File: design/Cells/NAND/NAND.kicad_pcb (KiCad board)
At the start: 2 copper layers, 4 parts, among them Q3 Q_NJFET_GSD, Q4 Q_NJFET_GSD, Q5 Q_PJFET_GSD, Q6 Q_PJFET_GSD

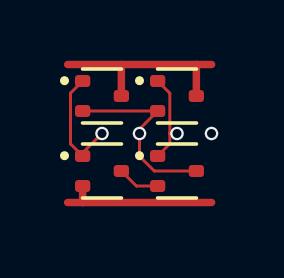
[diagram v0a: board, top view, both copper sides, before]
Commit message: Swap A and B pads in NAND footprint Polishing of AOI22 PCB, proper placement of the pins
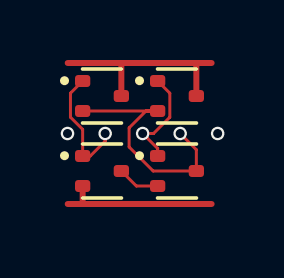
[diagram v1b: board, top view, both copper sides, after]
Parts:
- renumbered Q3 to N1, Q4 to N2, Q6 to P1, Q5 to P2
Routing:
- net Y: track 6.36 -> 8.37 mm
- net (no net): vias 1 -> 2
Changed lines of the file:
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@@
 		(descr "SOT523, https://www.diodes.com/assets/Package-Files/SOT523.pdf")
 		(tags "SOT-523")
-		(property "Reference" "Q4"
+		(property "Reference" "N2"
 			(at 0 -1.7 0)
 			(layer "F.SilkS")
@@
 		(descr "SOT523, https://www.diodes.com/assets/Package-Files/SOT523.pdf")
 		(tags "SOT-523")
-		(property "Reference" "Q5"
+		(property "Reference" "P2"
 			(at 0 -1.7 0)
 			(layer "F.SilkS")
@@
 		(descr "SOT523, https://www.diodes.com/assets/Package-Files/SOT523.pdf")
 		(tags "SOT-523")
-		(property "Reference" "Q3"
+		(property "Reference" "N1"
 			(at 0 -1.7 0)
 			(layer "F.SilkS")
@@
 		(descr "SOT523, https://www.diodes.com/assets/Package-Files/SOT523.pdf")
 		(tags "SOT-523")
-		(property "Reference" "Q6"
+		(property "Reference" "P1"
 			(at 0 -1.7 0)
 			(layer "F.SilkS")
@@
 	)
 	(via
-		(at 4.795 2.3)
+		(at 5 2.3)
 		(size 0.45)
 		(drill 0.3)
@@
 		(net 0)
 	)
-	(segment
-		(start 2.395 3.057738)
-		(end 2.887262 3.55)
+	(via
+		(at -0.005 2.3)
+		(size 0.45)
+		(drill 0.3)
+		(layers "F.Cu" "B.Cu")
+		(net 0)
+	)
+	(segment
+		(start 4.29 3.55)
+		(end 4.29 2.84)
+		(width 0.1)
+		(layer "F.Cu")
+		(net 1)
+	)
+	(segment
+		(start 2.85 3.55)
+		(end 2.049 2.749)
+		(width 0.1)
+		(layer "F.Cu")
+		(net 1)
+	)
+	(segment
+		(start 4.29 2.84)
+		(end 3.75 2.3)
+		(width 0.1)
+		(layer "F.Cu")
+		(net 1)
+	)
+	(segment
+		(start 4.29 3.55)
+		(end 2.85 3.55)
 		(width 0.1)
 		(layer "F.Cu")
@@
 	)
 	(segment
-		(start 3 1.55)
-		(end 2.594 1.956)
+		(start 2.049 2.113189)
+		(end 2.612189 1.55)
 		(width 0.1)
 		(layer "F.Cu")
@@
 	)
 	(segment
-		(start 2.887262 3.55)
-		(end 4.29 3.55)
+		(start 2.612189 1.55)
+		(end 3 1.55)
 		(width 0.1)
 		(layer "F.Cu")
@@
 	)
 	(segment
-		(start 2.594 1.956)
-		(end 2.395 2.155)
+		(start 2.049 2.749)
+		(end 2.049 2.113189)
 		(width 0.1)
 		(layer "F.Cu")
 		(net 1)
 	)
-	(segment
-		(start 2.395 2.155)
-		(end 2.395 3.057738)
-		(width 0.1)
-		(layer "F.Cu")
-		(net 1)
-	)
 	(via
-		(at 2.395 2.3)
+		(at 3.75 2.3)
 		(size 0.45)
 		(drill 0.3)
@@
 	)
 	(segment
-		(start 0.5 4.6)
-		(end 0 4.6)
-		(width 0.25)
+		(start 0.5 4.65)
+		(end 0 4.65)
+		(width 0.2)
 		(layer "F.Cu")
 		(net 2)
@@
 		(start 0.5 4.05)
 		(end 0.5 4.6)
-		(width 0.25)
+		(width 0.2)
 		(layer "F.Cu")
 		(net 2)
 	)
 	(segment
-		(start 0.5 4.6)
-		(end 4.8 4.6)
-		(width 0.25)
+		(start 0.5 4.65)
+		(end 4.8 4.65)
+		(width 0.2)
 		(layer "F.Cu")
 		(net 2)
 	)
 	(segment
-		(start 0.095 2.645)
+		(start 0.5 3.05)
+		(end 0.754999 3.05)
+		(width 0.1)
+		(layer "F.Cu")
+		(net 3)
+	)
+	(segment
+		(start 0.55 0.6)
+		(end 0.45 0.6)
+		(width 0.1)
+		(layer "F.Cu")
+		(net 3)
+	)
+	(segment
+		(start 0.5 2.162738)
 		(end 0.5 3.05)
 		(width 0.1)
@@
 	)
 	(segment
-		(start 0.095 0.955)
-		(end 0.095 2.645)
+		(start 0.754999 3.05)
+		(end 1.25 2.554999)
 		(width 0.1)
 		(layer "F.Cu")
@@
 	)
 	(segment
-		(start 0.5 2.945)
-		(end 1.145 2.3)
+		(start 0.45 0.6)
+		(end 0.094 0.956)
 		(width 0.1)
 		(layer "F.Cu")
@@
 	)
 	(segment
-		(start 0.5 3.05)
-		(end 0.5 2.945)
+		(start 0.5 0.55)
+		(end 0.55 0.6)
 		(width 0.1)
 		(layer "F.Cu")
@@
 	)
 	(segment
-		(start 0.5 0.55)
-		(end 0.095 0.955)
+		(start 0.094 1.756738)
+		(end 0.5 2.162738)
 		(width 0.1)
 		(layer "F.Cu")
 		(net 3)
 	)
+	(segment
+		(start 1.25 2.554999)
+		(end 1.25 2.3)
+		(width 0.1)
+		(layer "F.Cu")
+		(net 3)
+	)
+	(segment
+		(start 0.094 0.956)
+		(end 0.094 1.756738)
+		(width 0.1)
+		(layer "F.Cu")
+		(net 3)
+	)
 	(via
-		(at 1.145 2.3)
+		(at 1.25 2.3)
 		(size 0.45)
 		(drill 0.3)
@@
 		(start 4.29 0.954998)
 		(end 4.295 0.949998)
-		(width 0.1)
+		(width 0.2)
 		(layer "F.Cu")
 		(net 4)
@@
 		(start 4.29 0.01)
 		(end 4.3 0)
-		(width 0.25)
+		(width 0.2)
 		(layer "F.Cu")
 		(net 4)
 	)
 	(segment
-		(start 4.3 0)
-		(end 4.8 0)
-		(width 0.25)
+		(start 4.3 -0.05)
+		(end 4.8 -0.05)
+		(width 0.2)
 		(layer "F.Cu")
 		(net 4)
@@
 		(start 1.79 1.05)
 		(end 1.79 0.01)
-		(width 0.25)
+		(width 0.2)
 		(layer "F.Cu")
 		(net 4)
 	)
 	(segment
-		(start 1.8 0)
-		(end 4.3 0)
-		(width 0.25)
+		(start 1.8 -0.05)
+		(end 4.3 -0.05)
+		(width 0.2)
 		(layer "F.Cu")
 		(net 4)
@@
 		(start 4.29 1.05)
 		(end 4.29 0.01)
-		(width 0.25)
+		(width 0.2)
 		(layer "F.Cu")
 		(net 4)
@@
 		(start 4.29 1.05)
 		(end 4.29 0.954998)
-		(width 0.1)
+		(width 0.2)
 		(layer "F.Cu")
 		(net 4)
 	)
 	(segment
-		(start 1.8 0)
-		(end 0 0)
-		(width 0.25)
+		(start 1.8 -0.05)
+		(end 0 -0.05)
+		(width 0.2)
 		(layer "F.Cu")
 		(net 4)
@@
 	)
 	(segment
-		(start 3.406 2.644)
-		(end 3 3.05)
-		(width 0.1)
-		(layer "F.Cu")
-		(net 6)
-	)
-	(segment
-		(start 3.406 0.956)
-		(end 3.406 2.3)
-		(width 0.1)
-		(layer "F.Cu")
-		(net 6)
-	)
-	(segment
-		(start 3.406 2.3)
-		(end 3.406 2.644)
-		(width 0.1)
-		(layer "F.Cu")
-		(net 6)
-	)
-	(segment
-		(start 3.406 2.3)
-		(end 3.645 2.3)
-		(width 0.1)
-		(layer "F.Cu")
-		(net 6)
-	)
-	(segment
 		(start 3 0.55)
 		(end 3.406 0.956)
@@
 		(net 6)
 	)
+	(segment
+		(start 3 3.05)
+		(end 3 2.8)
+		(width 0.1)
+		(layer "F.Cu")
+		(net 6)
+	)
+	(segment
+		(start 3.406 1.756738)
+		(end 2.862738 2.3)
+		(width 0.1)
+		(layer "F.Cu")
+		(net 6)
+	)
+	(segment
+		(start 3 2.8)
+		(end 2.5 2.3)
+		(width 0.1)
+		(layer "F.Cu")
+		(net 6)
+	)
+	(segment
+		(start 3.406 0.956)
+		(end 3.406 1.756738)
+		(width 0.1)
+		(layer "F.Cu")
+		(net 6)
+	)
+	(segment
+		(start 2.862738 2.3)
+		(end 2.5 2.3)
+		(width 0.1)
+		(layer "F.Cu")
+		(net 6)
+	)
 	(via
-		(at 3.645 2.3)
+		(at 2.5 2.3)
 		(size 0.45)
 		(drill 0.3)

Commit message: All gates layout on a strict 2.5mm grid. Flipped versions of all three layouts
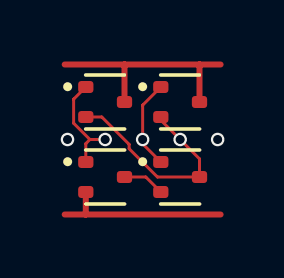
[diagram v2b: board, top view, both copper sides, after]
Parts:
- moved N1 0.23 mm to (1.25, 3.75)
- moved N2 0.23 mm to (3.75, 3.75)
- moved P1 0.23 mm to (1.25, 1.25)
- moved P2 0.23 mm to (3.75, 1.25)
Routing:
- net Y: track 8.37 -> 7.24 mm
- net A: track 4.15 -> 3.46 mm
- net VDD: track 7.10 -> 7.70 mm
- net GND: track 5.35 -> 5.95 mm
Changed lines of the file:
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@@
 	(footprint "Package_TO_SOT_SMD:SOT-523"
 		(layer "F.Cu")
-		(at 3.645 3.55)
+		(at 3.75 3.75)
 		(descr "SOT523, https://www.diodes.com/assets/Package-Files/SOT523.pdf")
 		(tags "SOT-523")
@@
 	(footprint "Package_TO_SOT_SMD:SOT-523"
 		(layer "F.Cu")
-		(at 3.645 1.05)
+		(at 3.75 1.25)
 		(descr "SOT523, https://www.diodes.com/assets/Package-Files/SOT523.pdf")
 		(tags "SOT-523")
@@
 	(footprint "Package_TO_SOT_SMD:SOT-523"
 		(layer "F.Cu")
-		(at 1.145 3.55)
+		(at 1.25 3.75)
 		(descr "SOT523, https://www.diodes.com/assets/Package-Files/SOT523.pdf")
 		(tags "SOT-523")
@@
 	(footprint "Package_TO_SOT_SMD:SOT-523"
 		(layer "F.Cu")
-		(at 1.145 1.05)
+		(at 1.25 1.25)
 		(descr "SOT523, https://www.diodes.com/assets/Package-Files/SOT523.pdf")
 		(tags "SOT-523")
@@
 	)
 	(via
-		(at 5 2.3)
+		(at 5 2.5)
 		(size 0.45)
 		(drill 0.3)
@@
 	)
 	(via
-		(at -0.005 2.3)
+		(at -0.005 2.5)
 		(size 0.45)
 		(drill 0.3)
@@
 	)
 	(segment
-		(start 4.29 3.55)
-		(end 4.29 2.84)
+		(start 2.992262 3.75)
+		(end 4.395 3.75)
 		(width 0.1)
 		(layer "F.Cu")
@@
 	)
 	(segment
-		(start 2.85 3.55)
-		(end 2.049 2.749)
+		(start 2.049 2.806738)
+		(end 2.992262 3.75)
 		(width 0.1)
 		(layer "F.Cu")
@@
 	)
 	(segment
-		(start 4.29 2.84)
-		(end 3.75 2.3)
+		(start 3.105 1.75)
+		(end 3.105 1.855)
 		(width 0.1)
 		(layer "F.Cu")
@@
 	)
 	(segment
-		(start 4.29 3.55)
-		(end 2.85 3.55)
+		(start 3.75 2.5)
+		(end 4.395 3.145)
 		(width 0.1)
 		(layer "F.Cu")
@@
 	)
 	(segment
-		(start 0.5 1.55)
-		(end 3 1.55)
+		(start 4.395 3.145)
+		(end 4.395 3.75)
 		(width 0.1)
 		(layer "F.Cu")
@@
 	)
 	(segment
-		(start 2.049 2.113189)
-		(end 2.612189 1.55)
+		(start 0.605 1.75)
+		(end 1.137811 1.75)
 		(width 0.1)
 		(layer "F.Cu")
@@
 	)
 	(segment
-		(start 2.612189 1.55)
-		(end 3 1.55)
+		(start 2.049 2.661189)
+		(end 2.049 2.806738)
 		(width 0.1)
 		(layer "F.Cu")
@@
 	)
 	(segment
-		(start 2.049 2.749)
-		(end 2.049 2.113189)
+		(start 1.137811 1.75)
+		(end 2.049 2.661189)
 		(width 0.1)
 		(layer "F.Cu")
 		(net 1)
 	)
+	(segment
+		(start 3.105 1.855)
+		(end 3.75 2.5)
+		(width 0.1)
+		(layer "F.Cu")
+		(net 1)
+	)
 	(via
-		(at 3.75 2.3)
+		(at 3.75 2.5)
 		(size 0.45)
 		(drill 0.3)
@@
 	)
 	(segment
-		(start 0.5 4.65)
-		(end 0 4.65)
+		(start 0.6 5)
+		(end 5.1 5)
 		(width 0.2)
 		(layer "F.Cu")
@@
 	)
 	(segment
-		(start 0.5 4.05)
-		(end 0.5 4.6)
+		(start -0.1 5)
+		(end 0.6 5)
 		(width 0.2)
 		(layer "F.Cu")
@@
 	)
 	(segment
-		(start 0.5 4.65)
-		(end 4.8 4.65)
+		(start 0.605 4.25)
+		(end 0.605 4.995)
 		(width 0.2)
 		(layer "F.Cu")
@@
 	)
 	(segment
-		(start 0.5 3.05)
-		(end 0.754999 3.05)
+		(start 0.605 4.995)
+		(end 0.6 5)
+		(width 0.2)
+		(layer "F.Cu")
+		(net 2)
+	)
+	(segment
+		(start 0.199 1.156)
+		(end 0.199 1.956738)
 		(width 0.1)
 		(layer "F.Cu")
@@
 	)
 	(segment
-		(start 0.55 0.6)
-		(end 0.45 0.6)
+		(start 0.742262 2.5)
+		(end 1.25 2.5)
 		(width 0.1)
 		(layer "F.Cu")
@@
 	)
 	(segment
-		(start 0.5 2.162738)
-		(end 0.5 3.05)
+		(start 0.605 0.75)
+		(end 0.199 1.156)
 		(width 0.1)
 		(layer "F.Cu")
@@
 	)
 	(segment
-		(start 0.754999 3.05)
-		(end 1.25 2.554999)
+		(start 0.199 1.956738)
+		(end 0.742262 2.5)
 		(width 0.1)
 		(layer "F.Cu")
@@
 	)
 	(segment
-		(start 0.45 0.6)
-		(end 0.094 0.956)
+		(start 0.742262 2.5)
+		(end 0.605 2.637262)
 		(width 0.1)
 		(layer "F.Cu")
@@
 	)
 	(segment
-		(start 0.5 0.55)
-		(end 0.55 0.6)
+		(start 0.605 2.637262)
+		(end 0.605 3.25)
 		(width 0.1)
 		(layer "F.Cu")
 		(net 3)
 	)
-	(segment
-		(start 0.094 1.756738)
-		(end 0.5 2.162738)
-		(width 0.1)
-		(layer "F.Cu")
-		(net 3)
-	)
-	(segment
-		(start 1.25 2.554999)
-		(end 1.25 2.3)
-		(width 0.1)
-		(layer "F.Cu")
-		(net 3)
-	)
-	(segment
-		(start 0.094 0.956)
-		(end 0.094 1.756738)
-		(width 0.1)
-		(layer "F.Cu")
-		(net 3)
-	)
 	(via
-		(at 1.25 2.3)
+		(at 1.25 2.5)
 		(size 0.45)
 		(drill 0.3)
@@
 	)
 	(segment
-		(start 1.79 0.955)
-		(end 1.795 0.95)
-		(width 0.1)
+		(start 4.395 0.005)
+		(end 4.4 0)
+		(width 0.2)
 		(layer "F.Cu")
 		(net 4)
 	)
 	(segment
-		(start 1.79 1.05)
-		(end 1.79 0.955)
-		(width 0.1)
+		(start 4.4 0)
+		(end 5.1 0)
+		(width 0.2)
 		(layer "F.Cu")
 		(net 4)
 	)
 	(segment
-		(start 4.29 0.954998)
-		(end 4.295 0.949998)
+		(start 1.895 1.25)
+		(end 1.895 0.005)
 		(width 0.2)
 		(layer "F.Cu")
@@
 	)
 	(segment
-		(start 4.29 0.01)
-		(end 4.3 0)
+		(start 4.395 1.25)
+		(end 4.395 0.005)
 		(width 0.2)
 		(layer "F.Cu")
@@
 	)
 	(segment
-		(start 4.3 -0.05)
-		(end 4.8 -0.05)
+		(start 1.9 0)
+		(end 4.4 0)
 		(width 0.2)
 		(layer "F.Cu")
@@
 	)
 	(segment
-		(start 1.79 1.05)
-		(end 1.79 0.01)
+		(start -0.1 0)
+		(end 1.9 0)
 		(width 0.2)
 		(layer "F.Cu")
@@
 	)
 	(segment
-		(start 1.8 -0.05)
-		(end 4.3 -0.05)
+		(start 1.895 0.005)
+		(end 1.9 0)
 		(width 0.2)
 		(layer "F.Cu")
@@
 	)
 	(segment
-		(start 4.29 1.05)
-		(end 4.29 0.01)
-		(width 0.2)
-		(layer "F.Cu")
-		(net 4)
-	)
-	(segment
-		(start 4.29 1.05)
-		(end 4.29 0.954998)
-		(width 0.2)
-		(layer "F.Cu")
-		(net 4)
-	)
-	(segment
-		(start 1.8 -0.05)
-		(end 0 -0.05)
-		(width 0.2)
-		(layer "F.Cu")
-		(net 4)
-	)
-	(segment
-		(start 3 4.05)
-		(end 2.29 4.05)
+		(start 1.895 3.75)
+		(end 2.605 3.75)
 		(width 0.1)
 		(layer "F.Cu")
@@
 	)
 	(segment
-		(start 2.29 4.05)
-		(end 1.79 3.55)
+		(start 2.605 3.75)
+		(end 3.105 4.25)
 		(width 0.1)
 		(layer "F.Cu")
@@
 	)
 	(segment
-		(start 3 0.55)
-		(end 3.406 0.956)
+		(start 2.5 2.5)
+		(end 2.5 2.645)
 		(width 0.1)
 		(layer "F.Cu")
@@
 	)
 	(segment
-		(start 3 3.05)
-		(end 3 2.8)
+		(start 3.105 0.75)
+		(end 2.5 1.355)
 		(width 0.1)
 		(layer "F.Cu")
@@
 	)
 	(segment
-		(start 3.406 1.756738)
-		(end 2.862738 2.3)
+		(start 2.5 1.355)
+		(end 2.5 2.5)
 		(width 0.1)
 		(layer "F.Cu")
@@
 	)
 	(segment
-		(start 3 2.8)
-		(end 2.5 2.3)
+		(start 2.5 2.645)
+		(end 3.105 3.25)
 		(width 0.1)
 		(layer "F.Cu")
 		(net 6)
 	)
-	(segment
-		(start 3.406 0.956)
-		(end 3.406 1.756738)
-		(width 0.1)
-		(layer "F.Cu")
-		(net 6)
-	)
-	(segment
-		(start 2.862738 2.3)
-		(end 2.5 2.3)
-		(width 0.1)
-		(layer "F.Cu")
-		(net 6)
-	)
 	(via
-		(at 2.5 2.3)
+		(at 2.5 2.5)
 		(size 0.45)
 		(drill 0.3)

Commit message: flip the cells to share power lines
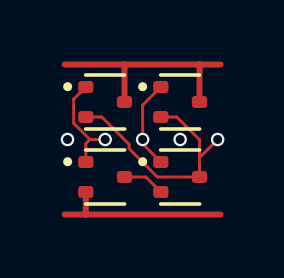
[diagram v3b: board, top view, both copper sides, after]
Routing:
- net Y: track 7.24 -> 9.16 mm
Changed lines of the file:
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@@
 	)
 	(via
-		(at 5 2.5)
+		(at 3.75 2.5)
 		(size 0.45)
 		(drill 0.3)
@@
 	)
 	(segment
+		(start 4.395 3.75)
+		(end 4.395 2.507189)
+		(width 0.1)
+		(layer "F.Cu")
+		(net 1)
+	)
+	(segment
 		(start 2.992262 3.75)
 		(end 4.395 3.75)
+		(width 0.1)
+		(layer "F.Cu")
+		(net 1)
+	)
+	(segment
+		(start 4.395 3.75)
+		(end 4.395 3.105)
 		(width 0.1)
 		(layer "F.Cu")
@@
 	)
 	(segment
-		(start 3.75 2.5)
-		(end 4.395 3.145)
-		(width 0.1)
-		(layer "F.Cu")
-		(net 1)
-	)
-	(segment
-		(start 4.395 3.145)
-		(end 4.395 3.75)
-		(width 0.1)
-		(layer "F.Cu")
-		(net 1)
-	)
-	(segment
 		(start 0.605 1.75)
 		(end 1.137811 1.75)
@@
 	)
 	(segment
+		(start 3.637811 1.75)
+		(end 3.105 1.75)
+		(width 0.1)
+		(layer "F.Cu")
+		(net 1)
+	)
+	(segment
 		(start 1.137811 1.75)
 		(end 2.049 2.661189)
@@
 	)
 	(segment
-		(start 3.105 1.855)
-		(end 3.75 2.5)
+		(start 4.395 2.507189)
+		(end 3.637811 1.75)
+		(width 0.1)
+		(layer "F.Cu")
+		(net 1)
+	)
+	(segment
+		(start 4.395 3.105)
+		(end 5 2.5)
 		(width 0.1)
 		(layer "F.Cu")
@@
 	)
 	(via
-		(at 3.75 2.5)
+		(at 5 2.5)
 		(size 0.45)
 		(drill 0.3)
